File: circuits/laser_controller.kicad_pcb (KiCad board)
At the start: 4 copper layers, 173 x 61.1 mm, 181 parts, among them J1 USB_MINI_B, J2 USB_MINI_B, J5 24V DC IN, J6 CONN_RJ45, J7 C192300, Q1 SOT-23, Q2 SOT-23, Q3 SOT-23, Q4 SOT-23, Q5 SOT-23, Q6 SOT-23, SW1 SW_PUSH, SW2 SW_PUSH, SW3 SW_PUSH, U1 SOIC-8_3.9x4.9mm_P1.27mm, U10 QFN-28-1EP_5x5mm_P0.5mm_EP3.3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, U11 SOT-23-5, U12 TSSOP-14_4.4x5mm_P0.65mm, U13 SOT-23, U14 LQFP-64_10x10mm_P0.5mm, U15 TSOT-23-6, U16 TSOT-23-6, U2 SOIC-8_3.9x4.9mm_P1.27mm, U3 SOIC-8_3.9x4.9mm_P1.27mm, U4 SOIC-8_3.9x4.9mm_P1.27mm, U5 SOT-23-5, U6 SOT-23-5, U7 SOT-23-5, U8 SOT-23-5, U9 ESP32-S3-WROOM-1

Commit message: Mirror power rails on 4x2 header
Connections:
- J7 pad 2: VIN_24V -> GND
- J7 pad 3: +5V -> +3V3
- J7 pad 5: PWM1 -> +5V
- J7 pad 6: PWM2 -> +5V
- J7 pad 7: PWM3 -> VIN_24V
- J7 pad 8: PWM4 -> VIN_24V
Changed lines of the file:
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@@
     (tags "C192300 BOOMELE 2.54-2*4P SMT SMD pin header")
     (attr smd)
-    (fp_text reference "J7" (at 3.81 -2.1) (layer "F.SilkS")
+    (fp_text reference "J7" (at 1.27 -2.1) (layer "F.SilkS")
         (effects (font (size 1 1) (thickness 0.15)))
     )
-    (fp_text value "C192300" (at 3.81 4.8) (layer "F.Fab")
+    (fp_text value "C192300" (at 1.27 10.65) (layer "F.Fab")
         (effects (font (size 1 1) (thickness 0.15)))
     )
-    (fp_text user "${REFERENCE}" (at 3.81 1.27) (layer "F.Fab")
+    (fp_text user "${REFERENCE}" (at 1.27 3.81) (layer "F.Fab")
         (effects (font (size 1 1) (thickness 0.15)))
     )
-    (fp_text user "C192300" (at 3.81 3.65) (layer "F.Fab")
+    (fp_text user "C192300" (at 1.27 8.7) (layer "F.Fab")
         (effects (font (size 0.8 0.8) (thickness 0.12)))
     )
-    (fp_line (start -1.2 -1.2) (end 8.82 -1.2)
+    (fp_line (start -1.2 -1.2) (end 3.74 -1.2)
       (stroke (width 0.12) (type solid)) (layer "F.SilkS"))
-    (fp_line (start -1.2 -1.2) (end -1.2 3.74)
+    (fp_line (start -1.2 -1.2) (end -1.2 8.82)
       (stroke (width 0.12) (type solid)) (layer "F.SilkS"))
-    (fp_line (start -1.2 3.74) (end 8.82 3.74)
+    (fp_line (start -1.2 8.82) (end 3.74 8.82)
       (stroke (width 0.12) (type solid)) (layer "F.SilkS"))
-    (fp_line (start 8.82 -1.2) (end 8.82 3.74)
+    (fp_line (start 3.74 -1.2) (end 3.74 8.82)
       (stroke (width 0.12) (type solid)) (layer "F.SilkS"))
     (fp_line (start -1.7 -1.7) (end -0.7 -1.7)
@@
     (fp_line (start -1.7 -1.7) (end -1.7 -0.7)
       (stroke (width 0.12) (type solid)) (layer "F.SilkS"))
-    (fp_line (start -1.9 -1.9) (end 9.52 -1.9)
+    (fp_line (start -1.9 -1.9) (end 4.44 -1.9)
       (stroke (width 0.05) (type solid)) (layer "F.CrtYd"))
-    (fp_line (start -1.9 4.44) (end -1.9 -1.9)
+    (fp_line (start -1.9 9.52) (end -1.9 -1.9)
       (stroke (width 0.05) (type solid)) (layer "F.CrtYd"))
-    (fp_line (start 9.52 -1.9) (end 9.52 4.44)
+    (fp_line (start 4.44 -1.9) (end 4.44 9.52)
       (stroke (width 0.05) (type solid)) (layer "F.CrtYd"))
-    (fp_line (start 9.52 4.44) (end -1.9 4.44)
+    (fp_line (start 4.44 9.52) (end -1.9 9.52)
       (stroke (width 0.05) (type solid)) (layer "F.CrtYd"))
     (fp_line (start -1.2 -0.2) (end -0.2 -1.2)
       (stroke (width 0.1) (type solid)) (layer "F.Fab"))
-    (fp_line (start -1.2 -0.2) (end -1.2 3.74)
+    (fp_line (start -1.2 -0.2) (end -1.2 8.82)
       (stroke (width 0.1) (type solid)) (layer "F.Fab"))
-    (fp_line (start -1.2 3.74) (end 8.82 3.74)
+    (fp_line (start -1.2 8.82) (end 3.74 8.82)
       (stroke (width 0.1) (type solid)) (layer "F.Fab"))
-    (fp_line (start -0.2 -1.2) (end 8.82 -1.2)
+    (fp_line (start -0.2 -1.2) (end 3.74 -1.2)
       (stroke (width 0.1) (type solid)) (layer "F.Fab"))
-    (fp_line (start 8.82 -1.2) (end 8.82 3.74)
+    (fp_line (start 3.74 -1.2) (end 3.74 8.82)
       (stroke (width 0.1) (type solid)) (layer "F.Fab"))
     (pad "1" smd roundrect (at 0 0) (size 1.6 1.8) (layers "F.Cu" "F.Paste" "F.Mask") (roundrect_rratio 0.15)
       (net 46 "GND"))
     (pad "2" smd roundrect (at 2.54 0) (size 1.6 1.8) (layers "F.Cu" "F.Paste" "F.Mask") (roundrect_rratio 0.15)
+      (net 46 "GND"))
+    (pad "3" smd roundrect (at 0 2.54) (size 1.6 1.8) (layers "F.Cu" "F.Paste" "F.Mask") (roundrect_rratio 0.15)
+      (net 1 "+3V3"))
+    (pad "4" smd roundrect (at 2.54 2.54) (size 1.6 1.8) (layers "F.Cu" "F.Paste" "F.Mask") (roundrect_rratio 0.15)
+      (net 1 "+3V3"))
+    (pad "5" smd roundrect (at 0 5.08) (size 1.6 1.8) (layers "F.Cu" "F.Paste" "F.Mask") (roundrect_rratio 0.15)
+      (net 2 "+5V"))
+    (pad "6" smd roundrect (at 2.54 5.08) (size 1.6 1.8) (layers "F.Cu" "F.Paste" "F.Mask") (roundrect_rratio 0.15)
+      (net 2 "+5V"))
+    (pad "7" smd roundrect (at 0 7.62) (size 1.6 1.8) (layers "F.Cu" "F.Paste" "F.Mask") (roundrect_rratio 0.15)
       (net 115 "VIN_24V"))
-    (pad "3" smd roundrect (at 5.08 0) (size 1.6 1.8) (layers "F.Cu" "F.Paste" "F.Mask") (roundrect_rratio 0.15)
-      (net 2 "+5V"))
-    (pad "4" smd roundrect (at 7.62 0) (size 1.6 1.8) (layers "F.Cu" "F.Paste" "F.Mask") (roundrect_rratio 0.15)
-      (net 1 "+3V3"))
-    (pad "5" smd roundrect (at 0 2.54) (size 1.6 1.8) (layers "F.Cu" "F.Paste" "F.Mask") (roundrect_rratio 0.15)
-      (net 110 "PWM1"))
-    (pad "6" smd roundrect (at 2.54 2.54) (size 1.6 1.8) (layers "F.Cu" "F.Paste" "F.Mask") (roundrect_rratio 0.15)
-      (net 111 "PWM2"))
-    (pad "7" smd roundrect (at 5.08 2.54) (size 1.6 1.8) (layers "F.Cu" "F.Paste" "F.Mask") (roundrect_rratio 0.15)
-      (net 112 "PWM3"))
-    (pad "8" smd roundrect (at 7.62 2.54) (size 1.6 1.8) (layers "F.Cu" "F.Paste" "F.Mask") (roundrect_rratio 0.15)
-      (net 113 "PWM4"))
+    (pad "8" smd roundrect (at 2.54 7.62) (size 1.6 1.8) (layers "F.Cu" "F.Paste" "F.Mask") (roundrect_rratio 0.15)
+      (net 115 "VIN_24V"))
     (model "${KIPRJMOD}/packages3d/Connector_PinHeader.3dshapes/PinHeader_2x04_P2.54mm_SMD_Vertical_C192300.step"
       (offset (xyz 0 0 0))

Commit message: Regenerate JLCPCB fab package
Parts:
- moved J7 4.20 mm to (116.3, 127.6)
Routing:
- net +3V3: track 86.2 -> 125.7 mm, vias 13 -> 15
- net VIN_24V: track 125.8 -> 152.7 mm
- net +5V: track 121.5 -> 134.5 mm
- net GND: track 232.7 -> 238.8 mm, vias 100 -> 102
- net /POWER_IO/MPD_BIAS: track 49.2 -> 45.7 mm
- net PWM1: track 146.9 -> 147.6 mm
- net LASER_N2: track 21.3 -> 21.9 mm
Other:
- board text removed: "USB"
- board text removed: "USB UART"

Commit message: Checkpoint laser controller layout cleanup
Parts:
- C61, C62: value 1uF 100V -> 10uF 50V
- R61: value 274k FB -> 237k FB
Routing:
- net LASER_V+: track 187.8 -> 201.1 mm
- net ISENSE1: track 126.1 -> 134.4 mm
- net MPD_RAW3: track 129.1 -> 131.1 mm
- net /LASER_GREEN/FB: track 22.2 -> 23.4 mm
- net Net-(D3-A): track 23.6 -> 24.6 mm
- net ISENSE2: track 178.8 -> 179.6 mm
- net LASER_N3: track 17.8 -> 18.6 mm
- net PWM1: track 147.6 -> 148.4 mm
- net /MCU_ESP32-S3/D-: track 21.7 -> 20.9 mm, vias 2 -> 0
- net LASER_N2: track 21.9 -> 21.3 mm
- net /MCU_ESP32-S3/DTR: track 8.83 -> 8.66 mm, vias 2 -> 3
- net Net-(U10-~{RST}): vias 3 -> 2

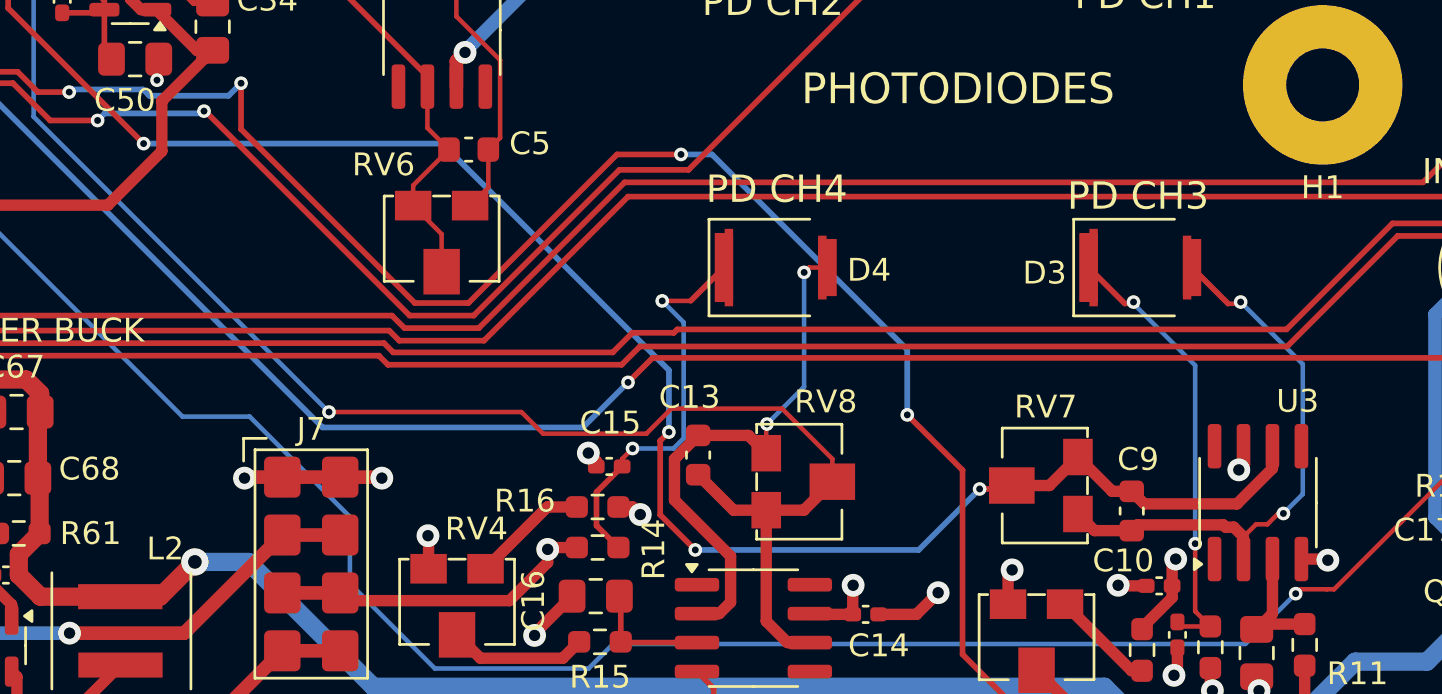
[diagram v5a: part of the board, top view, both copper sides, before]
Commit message: Fix sensitive TIA PCB routing
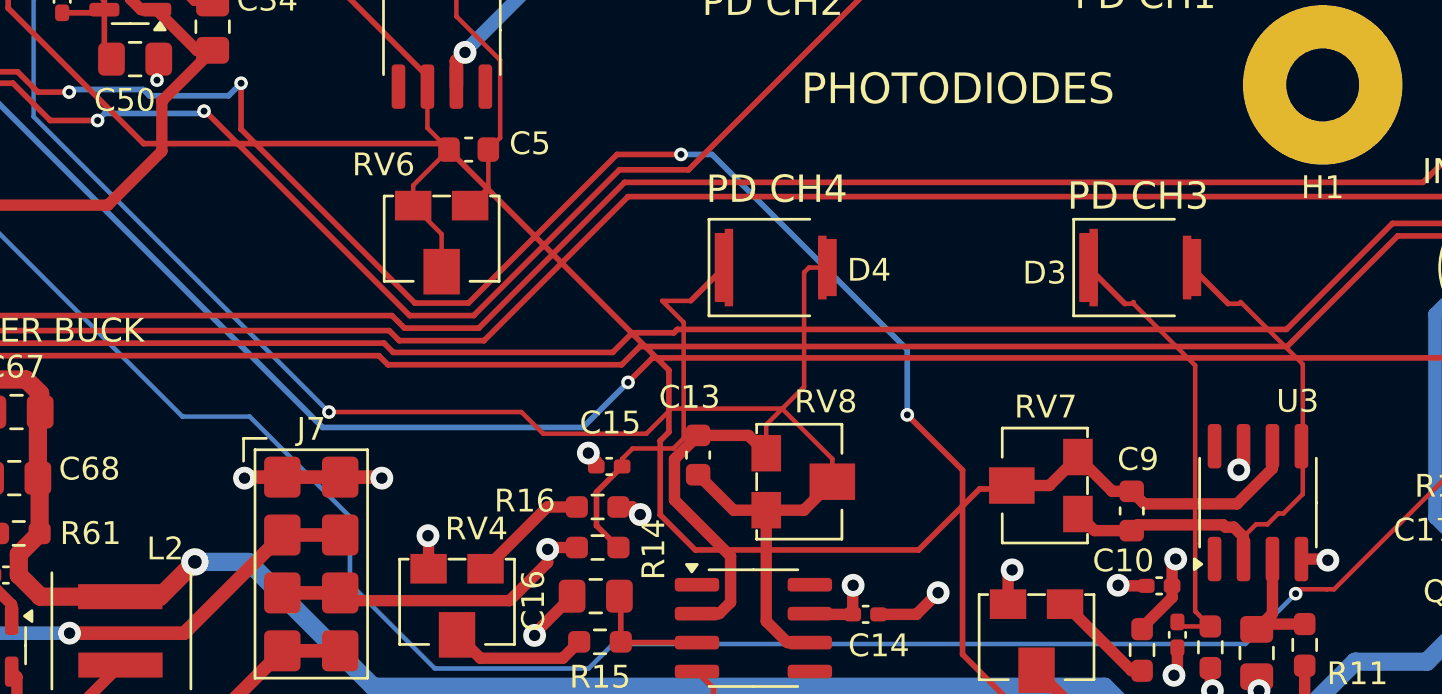
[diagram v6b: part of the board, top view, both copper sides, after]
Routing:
- net Net-(D4-K): vias 2 -> 0
- net VOUT3: vias 4 -> 0
- net Net-(D4-A): vias 2 -> 0
- net Net-(D3-K): vias 2 -> 0
- net Net-(D3-A): vias 2 -> 0
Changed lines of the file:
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@@
   (segment (start 151.8905 129.978) (end 151.1615 129.249) (width 0.5) (layer "F.Cu") (net 70))
   (segment (start 157.999999 129.825) (end 157.63934 129.825) (width 0.5) (layer "F.Cu") (net 70))
-  (via (at 158.3 119.95) (size 0.6) (drill 0.3) (layers "F.Cu" "B.Cu") (net 70))
-  (via (at 160.175 129.225) (size 0.6) (drill 0.3) (layers "F.Cu" "B.Cu") (net 70))
-  (segment (start 161.025 128.375) (end 160.175 129.225) (width 0.2) (layer "B.Cu") (net 70))
-  (segment (start 158.3 119.95) (end 161.025 122.675) (width 0.2) (layer "B.Cu") (net 70))
-  (segment (start 161.025 122.675) (end 161.025 128.375) (width 0.2) (layer "B.Cu") (net 70))
+  (segment (start 161.025 128.375) (end 160.175 129.225) (width 0.2) (layer "F.Cu") (net 70))
+  (segment (start 158.3 119.95) (end 161.025 122.675) (width 0.2) (layer "F.Cu") (net 70))
+  (segment (start 161.025 122.675) (end 161.025 128.375) (width 0.2) (layer "F.Cu") (net 70))
   (segment (start 153.525 120.025) (end 153.6 119.95) (width 0.2) (layer "F.Cu") (net 71))
   (segment (start 155.7235 134.181) (end 155.525 133.9825) (width 0.2) (layer "F.Cu") (net 71))
@@
   (segment (start 153.2225 120.025) (end 153.525 120.025) (width 0.2) (layer "F.Cu") (net 71))
   (segment (start 156.305 133.5155) (end 156.9705 134.181) (width 0.2) (layer "F.Cu") (net 71))
-  (via (at 153.6 119.95) (size 0.6) (drill 0.3) (layers "F.Cu" "B.Cu") (net 71))
-  (via (at 156.305 130.55) (size 0.6) (drill 0.3) (layers "F.Cu" "B.Cu") (net 71))
-  (segment (start 156.305 130.55) (end 156.305 122.73) (width 0.2) (layer "B.Cu") (net 71))
-  (segment (start 153.6 120.025) (end 153.6 119.95) (width 0.2) (layer "B.Cu") (net 71))
-  (segment (start 156.305 122.73) (end 153.6 120.025) (width 0.2) (layer "B.Cu") (net 71))
+  (segment (start 156.305 130.55) (end 156.305 122.73) (width 0.2) (layer "F.Cu") (net 71))
+  (segment (start 153.6 120.025) (end 153.6 119.95) (width 0.2) (layer "F.Cu") (net 71))
+  (segment (start 156.305 122.73) (end 153.6 120.025) (width 0.2) (layer "F.Cu") (net 71))
   (segment (start 135.424999 133.62) (end 135.925 133.119999) (width 0.5) (layer "F.Cu") (net 72))
   (segment (start 137.488 126.5815) (end 137.488 125.33063) (width 0.2) (layer "F.Cu") (net 72))
@@
   (segment (start 137.488 125.33063) (end 137.51863 125.3) (width 0.2) (layer "F.Cu") (net 72))
   (segment (start 136.7065 125.8) (end 137.488 126.5815) (width 0.5) (layer "F.Cu") (net 72))
-  (via (at 139.15 118.65) (size 0.6) (drill 0.3) (layers "F.Cu" "B.Cu") (net 72))
-  (via (at 137.51863 125.3) (size 0.6) (drill 0.3) (layers "F.Cu" "B.Cu") (net 72))
-  (segment (start 139.15 123.66863) (end 137.51863 125.3) (width 0.2) (layer "B.Cu") (net 72))
-  (segment (start 139.15 118.65) (end 139.15 123.66863) (width 0.2) (layer "B.Cu") (net 72))
+  (segment (start 139.15 123.66863) (end 137.51863 125.3) (width 0.2) (layer "F.Cu") (net 72))
+  (segment (start 139.15 118.65) (end 139.15 123.66863) (width 0.2) (layer "F.Cu") (net 72))
   (segment (start 130.0415 128.2875) (end 131.167 127.162) (width 0.25) (layer "F.Cu") (net 73))
   (segment (start 134.172499 119.900001) (end 132.925 119.900001) (width 0.2) (layer "F.Cu") (net 73))
@@
   (segment (start 131.167 126.833) (end 131.625 126.375) (width 0.2) (layer "F.Cu") (net 73))
   (segment (start 131.004 130.718) (end 130.0415 129.7555) (width 0.25) (layer "F.Cu") (net 73))
-  (via (at 132.925 119.900001) (size 0.6) (drill 0.3) (layers "F.Cu" "B.Cu") (net 73))
-  (via (at 131.625 126.375) (size 0.6) (drill 0.3) (layers "F.Cu" "B.Cu") (net 73))
-  (segment (start 133.867587 125.924326) (end 133.416913 126.375) (width 0.2) (layer "B.Cu") (net 73))
-  (segment (start 133.867587 120.842588) (end 133.867587 125.924326) (width 0.2) (layer "B.Cu") (net 73))
-  (segment (start 132.925 119.900001) (end 133.867587 120.842588) (width 0.2) (layer "B.Cu") (net 73))
-  (segment (start 133.416913 126.375) (end 131.625 126.375) (width 0.2) (layer "B.Cu") (net 73))
+  (segment (start 133.867587 125.924326) (end 133.416913 126.375) (width 0.2) (layer "F.Cu") (net 73))
+  (segment (start 133.867587 120.842588) (end 133.867587 125.924326) (width 0.2) (layer "F.Cu") (net 73))
+  (segment (start 132.925 119.900001) (end 133.867587 120.842588) (width 0.2) (layer "F.Cu") (net 73))
+  (segment (start 133.416913 126.375) (end 131.625 126.375) (width 0.2) (layer "F.Cu") (net 73))
   (segment (start 39.975 86.175) (end 42.25 86.175) (width 0.25) (layer "F.Cu") (net 74))
   (segment (start 42.25 86.175) (end 43.475 84.95) (width 0.25) (layer "F.Cu") (net 74))
@@
   (segment (start 148.1105 128.15) (end 148.2615 127.999) (width 0.25) (layer "F.Cu") (net 118))
   (segment (start 159.695 127.249999) (end 159.695 126.275) (width 0.5) (layer "F.Cu") (net 118))
-  (via (at 134.375 130.825) (size 0.6) (drill 0.3) (layers "F.Cu" "B.Cu") (net 118))
-  (via (at 110.175 113) (size 0.6) (drill 0.3) (layers "F.Cu" "B.Cu") (net 118))
-  (via (at 133.217587 125.655087) (size 0.6) (drill 0.3) (layers "F.Cu" "B.Cu") (net 118))
-  (via (at 146.85 128.15) (size 0.6) (drill 0.3) (layers "F.Cu" "B.Cu") (net 118))
-  (segment (start 133.217587 122.937992) (end 133.217587 125.655087) (width 0.25) (layer "B.Cu") (net 118))
-  (segment (start 134.375 130.825) (end 144.175 130.825) (width 0.25) (layer "B.Cu") (net 118))
-  (segment (start 123.279595 113) (end 133.217587 122.937992) (width 0.25) (layer "B.Cu") (net 118))
-  (segment (start 144.175 130.825) (end 146.85 128.15) (width 0.25) (layer "B.Cu") (net 118))
-  (segment (start 110.175 113) (end 123.279595 113) (width 0.25) (layer "B.Cu") (net 118))
+  (segment (start 133.217587 122.937992) (end 133.217587 125.655087) (width 0.25) (layer "F.Cu") (net 118))
+  (segment (start 134.375 130.825) (end 144.175 130.825) (width 0.25) (layer "F.Cu") (net 118))
+  (segment (start 123.279595 113) (end 133.217587 122.937992) (width 0.25) (layer "F.Cu") (net 118))
+  (segment (start 144.175 130.825) (end 146.85 128.15) (width 0.25) (layer "F.Cu") (net 118))
+  (segment (start 110.175 113) (end 123.279595 113) (width 0.25) (layer "F.Cu") (net 118))
   (segment (start 139.4 134.89) (end 138.425001 134.89) (width 0.5) (layer "F.Cu") (net 119))
   (segment (start 126.75 124.775) (end 118.306399 124.775) (width 0.2) (layer "F.Cu") (net 119))
